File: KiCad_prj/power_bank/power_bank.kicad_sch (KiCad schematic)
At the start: 2 parts, among them U2 TPS54560BDDA, U4 TPS54560BDDA

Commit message: power_bank: dokonceny navrh schema
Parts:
- removed U2, U4: TPS54560BDDA, Package_SO:Texas_R-PDSO-G8_EP2.95x4.9mm_Mask2.4x3.1mm_ThermalVias, symbol Regulator_Switching:TPS54560BDDA
- added C1, C3, C5, C7: 330n, symbol Device:C
- added C10, C11, C12, C13, C2, C4, C6: 10u, symbol Device:C
- added C8: 33p, symbol Device:C
- added C9: 100n, symbol Device:C
- added D1: BZX384B15-HE3_A08, Diode_SMD:D_SOD-323F, symbol Device:D_Zener
- added J1, J2: Conn_01x02_Socket, symbol Connector:Conn_01x02_Socket
- added L1: NRS6045T1R8NMGKV, symbol Device:L
- added L2: AMRM00101040220MA1, Inductor_SMD:L_10.4x10.4_H4.8, symbol Device:L
- added R1: 110k, Resistor_SMD:R_0805_2012Metric, symbol Device:R
- added R2: 15k, Resistor_SMD:R_0805_2012Metric, symbol Device:R
- added R3, R5: 47k, Resistor_SMD:R_0805_2012Metric, symbol Device:R
- added R4: 12k, Resistor_SMD:R_0805_2012Metric, symbol Device:R
- added R6, R8: 3k3, Resistor_SMD:R_0805_2012Metric, symbol Device:R
- added R7: 10k, Resistor_SMD:R_0805_2012Metric, symbol Device:R
- added U1: LMR51625, Package_TO_SOT_SMD:SOT-23-6, symbol switching_converters:LMR516x5
- added U2: TPS564242, Package_TO_SOT_SMD:SOT-563, symbol switching_converters:TPS564242
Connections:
- net Battery/BAT_POS: now also C11.1, C13.1, R7.1, U2.1 (VIN)
- net Battery/CHA_POS: now also C10.1, C12.1, L2.2, R5.1
- new net: C9.1, U1.6 (CB)
- new net: D1.2 (A), R3.1
- new net EN_IN: R3.2, R4.1, U1.2 (EN)
- new net EN_OUT: R7.2, R8.1, U2.5 (EN)
- new net FB_IN: R5.2, R6.1, U1.1 (FB)
- new net FB_OUT: C8.2, R1.2, R2.1, U2.6 (FB)
- new net GND: C11.2, C13.2, C2.2, C4.2, C6.2, J2.2 (Pin_2), R2.2, R8.2, U2.3 (GND), U2.4 (AGND)
- new net SWN_IN: C9.2, L2.1, U1.5 (SW)
- new net SWN_OUT: L1.2, U2.2 (SW)
- new net VIN_GND: C1.2, C10.2, C12.2, C3.2, C5.2, C7.2, J1.2 (Pin_2), R4.2, R6.2, U1.4 (GND)
- new net VIN_from_+20V_to_+50V: C1.1, C3.1, C5.1, C7.1, D1.1 (K), J1.1 (Pin_1), U1.3 (VIN)
- new net VOUT_+5V: C2.1, C4.1, C6.1, C8.1, J2.1 (Pin_1), L1.1, R1.1
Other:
- note added: "1.8uH"
- note added: "22uH"
- title: (none) -> ${TITLE}

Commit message: power_bank: doplnena pouzdra
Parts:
- added D3, D4: LED, LED_THT:LED_D3.0mm, symbol Device:LED
- added R19: 3k3, Resistor_SMD:R_0805_2012Metric, symbol Device:R
- added R20: 2k2, Resistor_SMD:R_0805_2012Metric, symbol Device:R
- C1, C10, C11, C12, C13, C2, C3, C4, C5, C6, C7, C8, C9: footprint (none) -> Capacitor_SMD:C_0805_2012Metric
- J1, J2: value Conn_01x02_Socket -> svorkovnice; footprint (none) -> Connector_Phoenix_MSTB:PhoenixContact_MSTBVA_2,5_2-G-5,08_1x02_P5.08mm_Vertical
- L1: value NRS6045T1R8NMGKV -> ASPI-6045S-1R8N-T; footprint (none) -> Inductor_SMD:L_APV_ANR6045
- R7: value 10k -> 100k
- R8: value 3k3 -> 22k
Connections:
- net Battery/CHA_POS: now also D3.2 (A)
- net GND: now also R20.1
- net VIN_GND: now also R19.1
- net VOUT_+5V: now also D4.2 (A)
- new net: D3.1 (K), R19.2
- new net: D4.1 (K), R20.2
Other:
- moved on the sheet: C1, C10, C11, C12, C13, C2, C3, C4, C5, C6, C7, C8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

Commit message: pocatek dps
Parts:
- added J3, J4: vypinac, Connector_PinHeader_2.54mm:PinHeader_1x02_P2.54mm_Vertical_SMD_Pin1Left, symbol Connector:Conn_01x02_Pin
- added JP1, JP2: Jumper, Jumper:SolderJumper-2_P1.3mm_Open_RoundedPad1.0x1.5mm, symbol Jumper:SolderJumper_2_Open
- added TP1: TestPoint, TestPoint:TestPoint_Loop_D1.80mm_Drill1.0mm_Beaded, symbol Connector:TestPoint
- renumbered D4 to D1, D1 to D2, R20 to R1, R19 to R10, R1 to R2, R2 to R3, R3 to R4, R4 to R5, R8 to R6, R5 to R7, R6 to R8, R7 to R9
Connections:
- net Battery/BAT_POS: now also R9.2; no longer R9.1
- net EN_IN: now also J3.2 (Pin_2), JP1.2 (B); no longer R4.2
- net EN_OUT: now also J4.2 (Pin_2), JP2.1 (A); no longer R9.2
- net VOUT_+5V: now also TP1.1
- new net: J4.1 (Pin_1), JP2.2 (B), R9.1
- new net: J3.1 (Pin_1), JP1.1 (A), R4.2
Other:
- moved on the sheet: R4, R6, R9

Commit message: power_bank: priprava pouzdra chladice
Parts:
- TP1: footprint TestPoint:TestPoint_Loop_D1.80mm_Drill1.0mm_Beaded -> TestPoint:TestPoint_Pad_D2.0mm
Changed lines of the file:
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@@
 			)
 		)
-		(property "Footprint" "TestPoint:TestPoint_Loop_D1.80mm_Drill1.0mm_Beaded"
+		(property "Footprint" "TestPoint:TestPoint_Pad_D2.0mm"
 			(at 90.17 87.63 0)
 			(effects

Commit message: power_bank: zakladni vzhled DPS
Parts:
- J3, J4: footprint Connector_PinHeader_2.54mm:PinHeader_1x02_P2.54mm_Vertical_SMD_Pin1Left -> Connector_PinHeader_2.54mm:PinHeader_1x02_P2.54mm_Vertical
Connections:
- net Battery/CHA_POS: now also R10.2; no longer D3.2 (A)
- net EN_IN: now also D2.2 (A); no longer J3.2 (Pin_2), JP1.2 (B)
- net GND: now also D1.1 (K); no longer R1.1
- net VIN_GND: now also D3.1 (K); no longer R10.1
- net VIN_from_+20V_to_+50V: now also J3.1 (Pin_1), JP1.1 (A); no longer D2.1 (K)
- net VOUT_+5V: now also R1.2; no longer D1.2 (A)
- net at R4.1: now also J3.2 (Pin_2), JP1.2 (B); no longer D2.2 (A)
- new net: D3.2 (A), R10.1
- new net: D1.2 (A), R1.1
- new net: D2.1 (K), R4.2
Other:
- moved on the sheet: D1, D2, D3, J3, JP1, R1, R10, R4

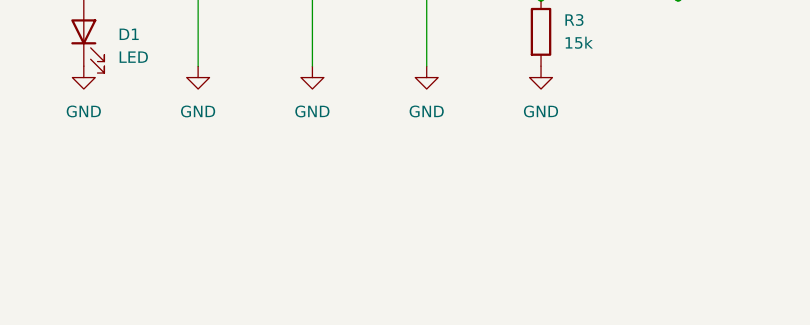
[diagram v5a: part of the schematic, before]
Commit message: power_bank: vyrobni rozmisteni prvku, doplnit uzivatelske popisky
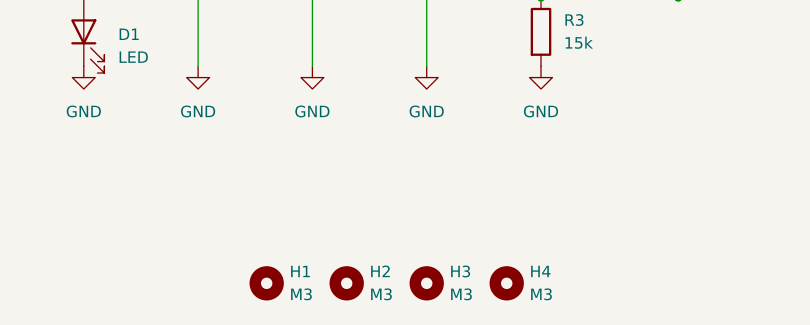
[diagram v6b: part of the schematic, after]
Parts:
- added H1, H2, H3, H4: M3, MountingHole:MountingHole_3.2mm_M3, symbol Mechanical:MountingHole

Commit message: Odeslano do vyroby, rev 1.0
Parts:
- added C21: 220n, Capacitor_SMD:C_0805_2012Metric, symbol Device:C
- C1, C3, C5, C7: value 330n -> 220n; JLCPCB Part # (none) -> C6119933
- C10, C11, C12, C13, C2, C4, C6: JLCPCB Part # (none) -> C15850
- C8: JLCPCB Part # (none) -> C107115
- C9: JLCPCB Part # (none) -> C28233
- D1, D3, J1, J2, J3, J4, TP1: now left out of the parts list
- D2: JLCPCB Part # (none) -> C49296788
- L1: JLCPCB Part # (none) -> C2997654
- L2: JLCPCB Part # (none) -> C10165
- R1: JLCPCB Part # (none) -> C17520
- R10, R8: JLCPCB Part # (none) -> C26010
- R2: JLCPCB Part # (none) -> C4310
- R3: JLCPCB Part # (none) -> C17475
- R4, R7: JLCPCB Part # (none) -> C17713
- R5: JLCPCB Part # (none) -> C17444
- R6: JLCPCB Part # (none) -> C17560
- R9: JLCPCB Part # (none) -> C149504
- U1: JLCPCB Part # (none) -> C45262767
- U2: JLCPCB Part # (none) -> C5219267
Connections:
- net VIN_GND: now also C21.2
- net VIN_from_+20V_to_+50V: now also C21.1

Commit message: Oprava objednavaciho kodu u power_bank
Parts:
- R2: JLCPCB Part # C4310 -> C17422
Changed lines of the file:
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@@
 			)
 		)
-		(property "JLCPCB Part #" "C4310"
+		(property "JLCPCB Part #" "C17422"
 			(at 97.79 91.44 0)
 			(effects
